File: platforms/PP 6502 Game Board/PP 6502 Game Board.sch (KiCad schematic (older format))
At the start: 33 parts, among them J1 BASE, J2 BTM, J3 TOP, J4 SBC, J5 TRS_3.5mm, M1 Mounting, M2 Mounting, M3 Mounting, M4 Mounting, Q1 2N2222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

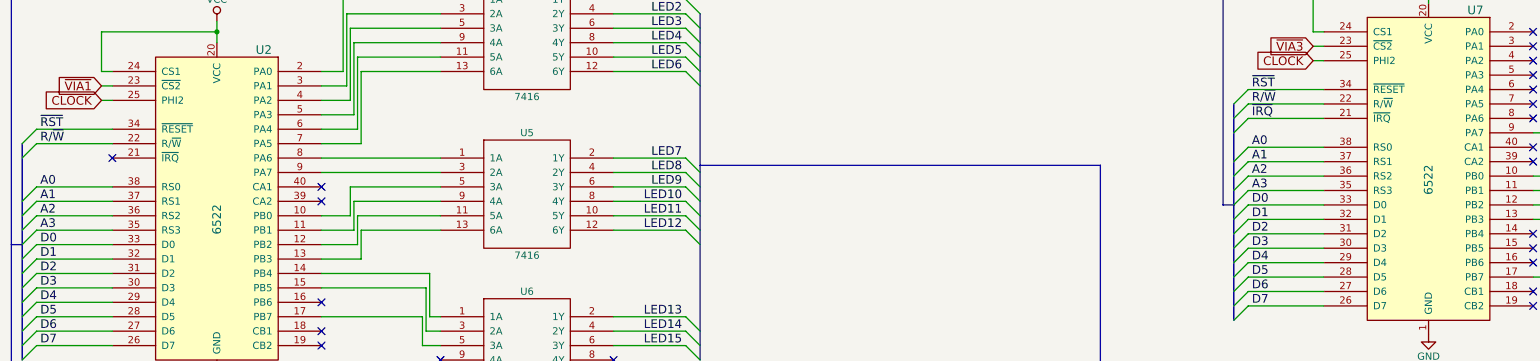
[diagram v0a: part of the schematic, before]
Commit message: Moved game board IRQ connection to correct VIA
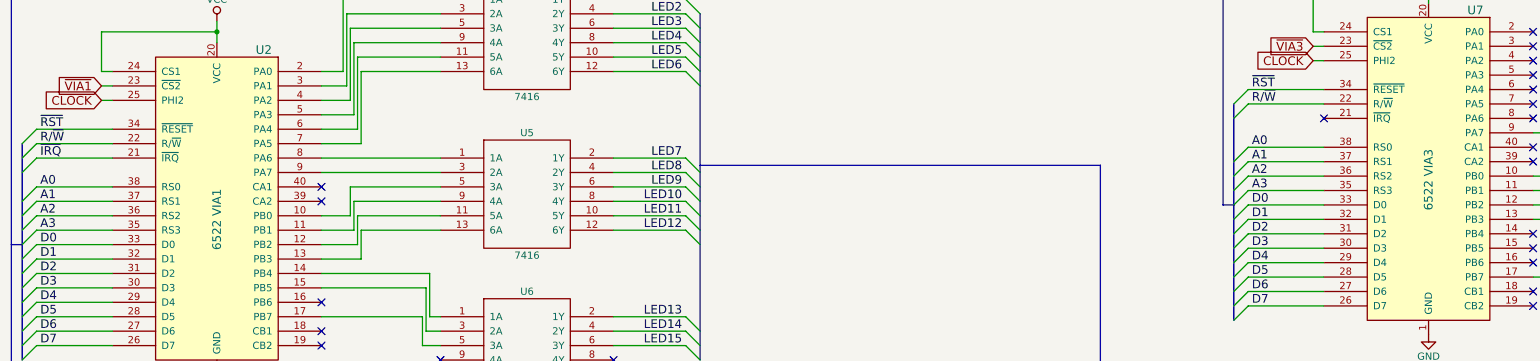
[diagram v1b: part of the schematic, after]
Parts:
- U2: value 6522 -> 6522 VIA1
- U7: value 6522 -> 6522 VIA3
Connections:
- net ~IRQ: now also U2.21 (~IRQ); no longer U7.21 (~IRQ)
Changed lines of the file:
@@
 P 2050 5050
 F 0 "U2" H 1725 6125 60  0000 C CNN
-F 1 "6522" V 2050 4950 60  0000 C CNN
+F 1 "6522 VIA1" V 2050 4950 60  0000 C CNN
 F 2 "Housings_DIP:DIP-40_W15.24mm_Socket_LongPads" H 1550 5250 60  0001 C CNN
 F 3 "" H 1550 5250 60  0000 C CNN
@@
 Text GLabel 1575 8125 2    60   Output ~ 0
 CLOCK
-NoConn ~ 1325 4725
+NoConn ~ 9725 4450
 Text GLabel 1250 4325 0    60   Input ~ 0
 CLOCK
@@
 P 10450 4775
 F 0 "U7" H 10125 5850 60  0000 C CNN
-F 1 "6522" V 10450 4675 60  0000 C CNN
+F 1 "6522 VIA3" V 10450 4675 60  0000 C CNN
 F 2 "Housings_DIP:DIP-40_W15.24mm_Socket_LongPads" H 9950 4975 60  0001 C CNN
 F 3 "" H 9950 4975 60  0000 C CNN
@@
 Wire Wire Line
 	12575 4550 13675 4550
-Text Label 9225 4450 0    60   ~ 0
+Text Label 825  4725 0    60   ~ 0
 ~IRQ
 Entry Wire Line
-	9200 4450 9100 4550
-Wire Wire Line
-	9200 4450 9725 4450
+	800  4725 700  4825
+Wire Wire Line
+	800  4725 1325 4725
 Text Label 14825 6075 0    60   ~ 0
 ~IRQ
